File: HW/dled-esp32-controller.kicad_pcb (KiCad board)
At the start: 2 copper layers, 53 x 43 mm, 35 parts, among them J1 PinsI2C, J2 PinsDbg, J3 DLED, J4 swRes, J5 PinsExp, J9 Power5V, Q1 STD46P4LLF6, Q2 IRLML2502, SW1 BootBtn, U1 ESP-WROOM-32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

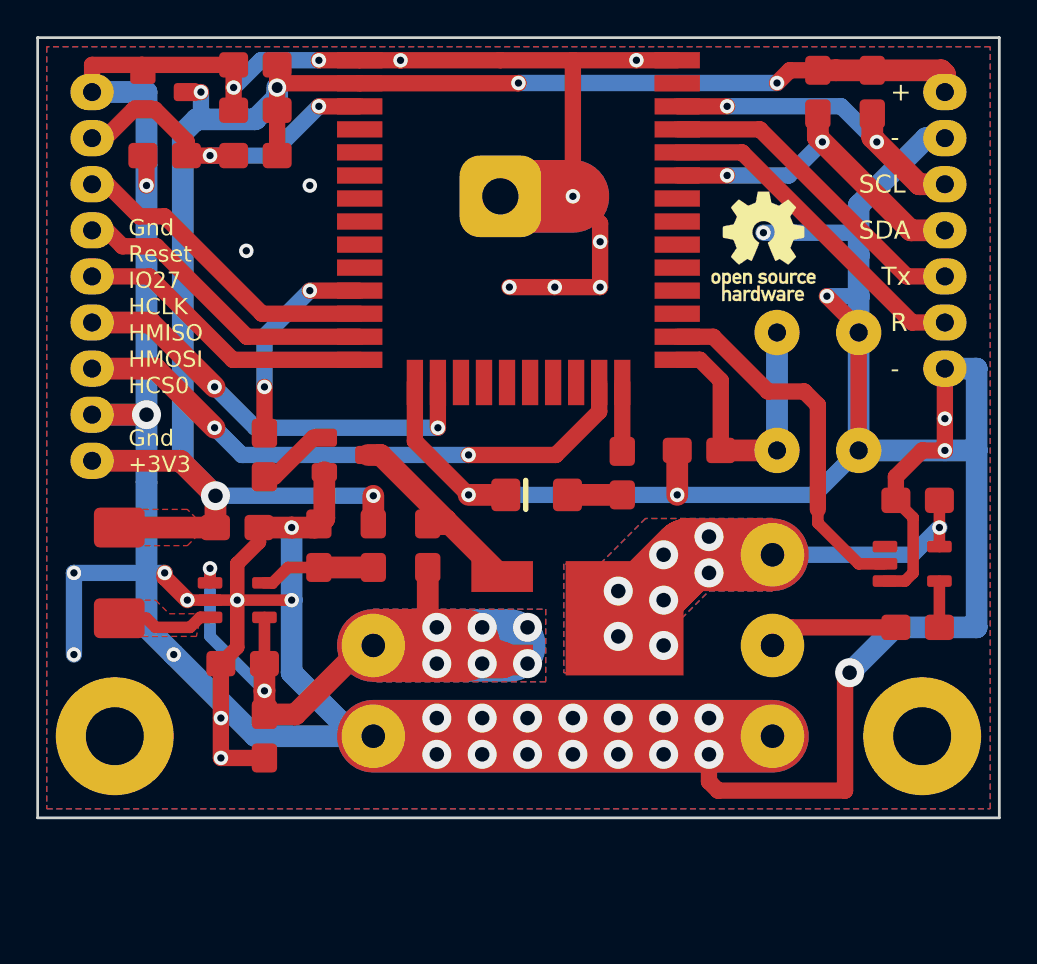
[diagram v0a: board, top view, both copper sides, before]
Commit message: Modifies the design for two outputs
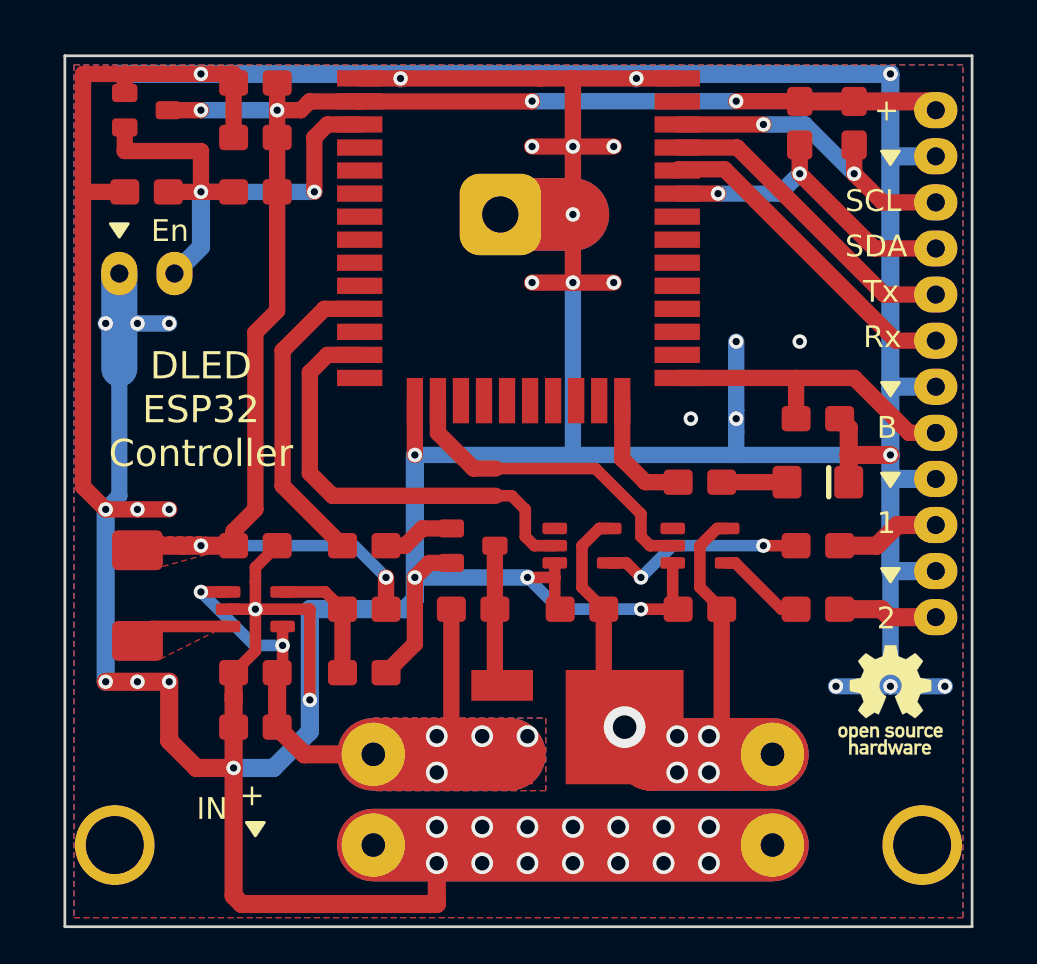
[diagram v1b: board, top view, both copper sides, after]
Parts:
- removed SW1: BootBtn, CalinGeneric:SW-Push-4
- added C9: 100nF, CalinGeneric:C0805HS, F.Cu at (60.0, 82.5)
- added J8: LEDpwr, CalinConnectors:DG301-5-2, F.Cu at (64.0, 93.0)
- added R10: 330, CalinGeneric:R0805HS, F.Cu at (66.5, 82.5)
- added U5: SN74LV1T34, CalinGeneric:SOT-23-5-HS, F.Cu at (60.0, 79.0)
- J3: value DLED -> BootBtn; footprint CalinConnectors:DG301-5-3 -> CalinConnectors:Pin_Header_Straight_1x02
- J5: value PinsExp -> LEDcmd; footprint CalinConnectors:Pin_Header_Straight_1x07 -> CalinConnectors:Pin_Header_Straight_1x03
- U2: value SN74LV1T34 -> BD48K28...30; footprint CalinGeneric:SOT-23-5-HS -> CalinGeneric:SOT-23-HS
- U4: value BD48K28...30 -> SN74LV1T34; footprint CalinGeneric:SOT-23-HS -> CalinGeneric:SOT-23-5-HS
- moved J5 50.1 mm to (73.0, 77.9)
- moved U2 49.0 mm to (29.5, 55.0)
- moved U4 34.0 mm to (53.5, 79.0)
- moved SYM1 26.0 mm to (70.5, 87.5)
- moved C5 19.4 mm to (53.5, 82.5)
- moved D1 15.5 mm to (66.5, 75.5), turned to 180 degrees
- moved J3 14.8 mm to (73.0, 72.8), turned to 0 degrees
- moved J4 8.73 mm to (31.0, 64.0), turned to 270 degrees
- moved Q2 8.60 mm to (47.5, 79.0)
- moved R7 7.43 mm to (41.5, 86.0), turned to 180 degrees
- moved R9 7.43 mm to (41.5, 79.0), turned to 180 degrees
- moved R5 7.11 mm to (66.5, 79.0), turned to 180 degrees
- moved C4 6.78 mm to (66.5, 72.0), turned to 0 degrees
- moved H1 6.00 mm to (27.8, 95.5)
- moved H2 6.00 mm to (72.2, 95.5)
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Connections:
- J3 pad 1: GND -> /Boot
- J3 pad 2: Net-(J3-Pad2) -> GND
- J5 pad 1: /IO27 -> /LEDo1
- J5 pad 2: /HSPICLK -> GND
- J5 pad 3: /HSPIQ -> /LEDo2
- R5 pad 1: Net-(J3-Pad2) -> /LEDo1
- U1 pad 12: /IO27 -> (no net)
- U1 pad 13: /HSPICLK -> /LEDc1
- U1 pad 14: /HSPIQ -> (no net)
- U1 pad 16: /HSPID -> /LEDc2
- U1 pad 23: /HSPICS0 -> (no net)
- U1 pad 26: /LEDcmd -> (no net)
- U2 pad 1: (no net) -> GND
- U2 pad 2: /LEDcmd -> /Reset
- U2 pad 3: GND -> +3V3
- U4 pad 1: GND -> (no net)
- U4 pad 2: /Reset -> /LEDc1
- U4 pad 3: +3V3 -> GND
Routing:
- net GND: track 348.4 -> 413.4 mm, vias 44 -> 49
- net /HSPICS0: track 32.5 -> 0.00 mm, vias 2 -> 0
- net /LEDc1: track 0.00 -> 24.7 mm
- net /HSPID: track 24.0 -> 0.00 mm, vias 2 -> 0
- net /LEDcmd: track 20.4 -> 0.00 mm
- net /LEDc2: track 0.00 -> 18.0 mm
- net /IO27: track 17.7 -> 0.00 mm
- net /HSPICLK: track 17.2 -> 0.00 mm
- net /HSPIQ: track 16.7 -> 0.00 mm
- net +5VL: track 36.4 -> 52.1 mm, vias 8 -> 5
- net +3V3: track 97.9 -> 87.3 mm
- net /Reset: track 19.6 -> 28.5 mm
- net Net-(R5-Pad2): track 2.55 -> 11.4 mm, vias 0 -> 2
- net Net-(J3-Pad2): track 7.21 -> 0.00 mm
- net /LEDo1: track 0.00 -> 5.77 mm
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- removed copper zone on B.Cu, net +5VL
- removed copper zone on F.Cu, net +5VL
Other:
- board size 53 x 43 mm -> 50 x 48 mm
- board text added: "1"
- board text added: "2"
- board text added: "B"
- board text added: "DLED ESP32 Controller"
- board text added: "En"
- board text added: "IN"
- board text added: "Rx"
- board text added: "github.com CalinRadoni dled-esp32-controller"
- board text removed: "-"
- board text removed: "DLED-ESP32-Controller"
- board text removed: "Gnd Reset IO27 HCLK HMISO HMOSI HCS0 Gnd +3V3"
- board text removed: "R"

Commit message: Adds an extension header and improves many PCB traces.
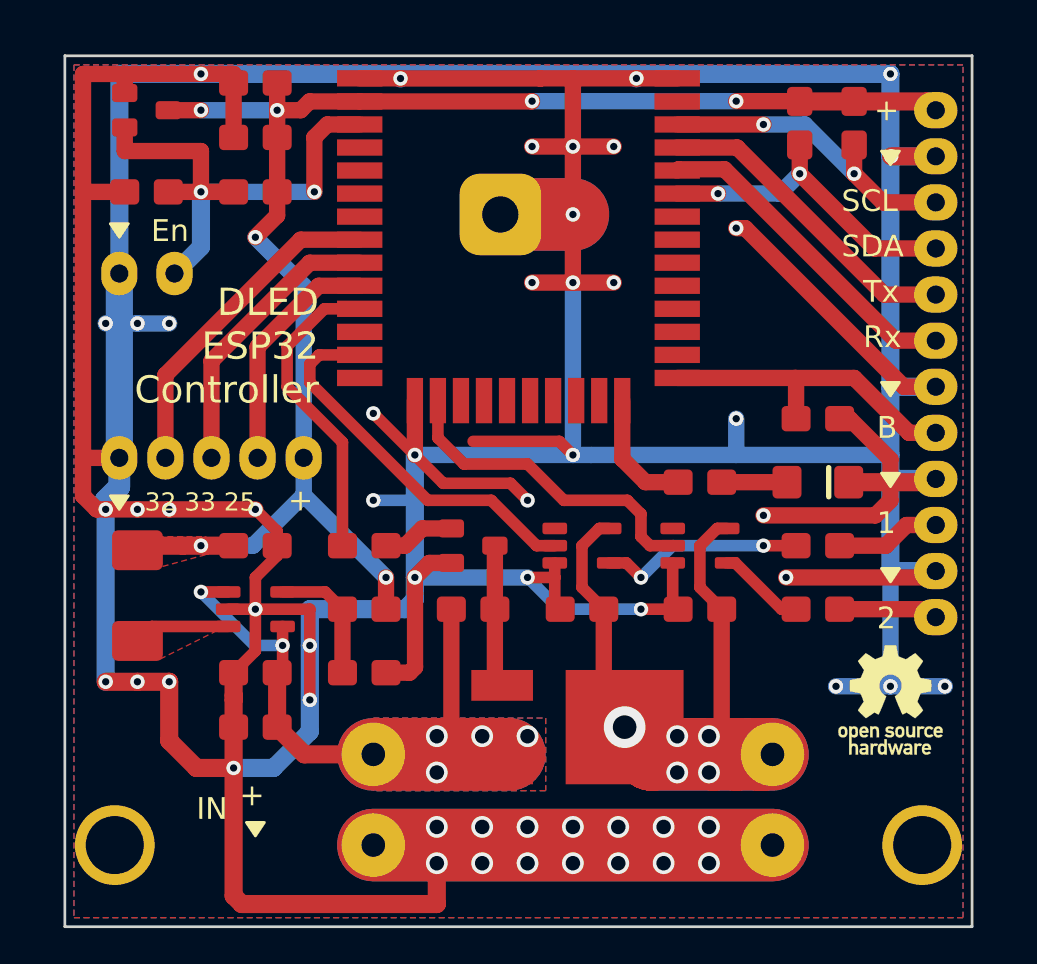
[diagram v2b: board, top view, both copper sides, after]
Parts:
- added J6: PinsExt, CalinConnectors:Pin_Header_Straight_1x05, F.Cu at (28.0, 74.2)
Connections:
- U1 pad 10: (no net) -> /25
- U1 pad 8: (no net) -> /32
- U1 pad 9: (no net) -> /33
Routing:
- net GND: track 413.4 -> 486.7 mm, vias 49 -> 55
- net /32: track 0.00 -> 18.4 mm
- net /33: track 0.00 -> 15.8 mm
- net /25: track 0.00 -> 13.1 mm
- net /LEDc1: track 24.7 -> 21.2 mm
- net +3V3: track 87.3 -> 87.4 mm, vias 6 -> 7
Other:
- board text added: "32 33 25"

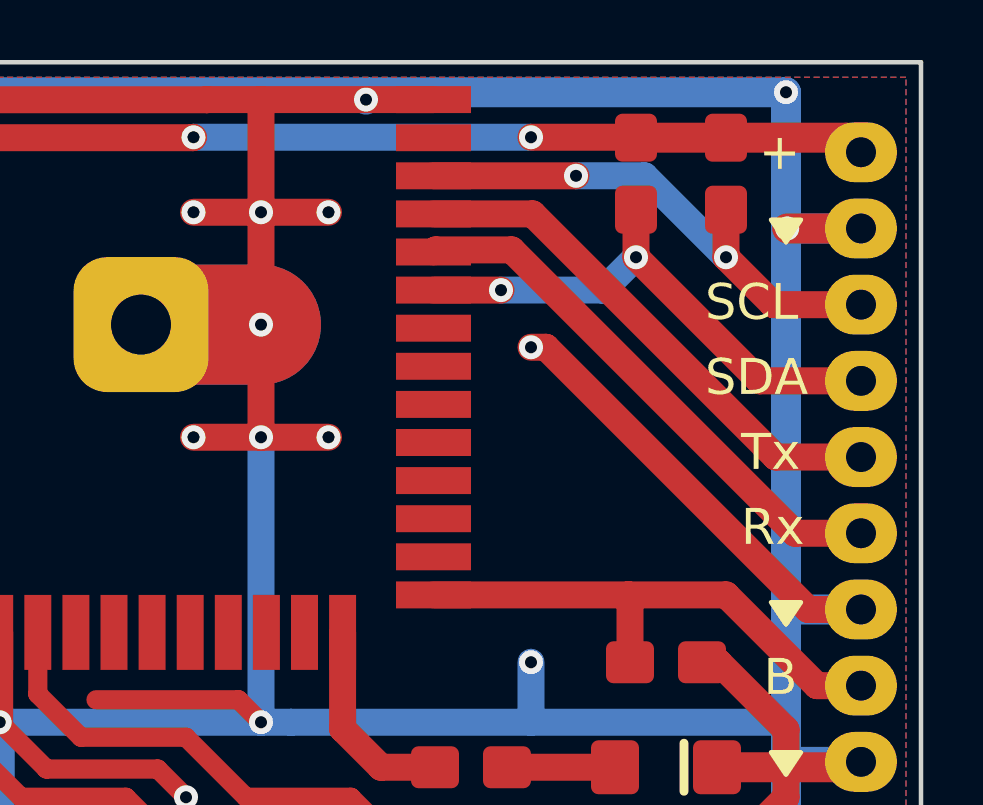
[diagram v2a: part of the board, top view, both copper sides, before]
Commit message: Rebuilds the PCB for the second extension connector
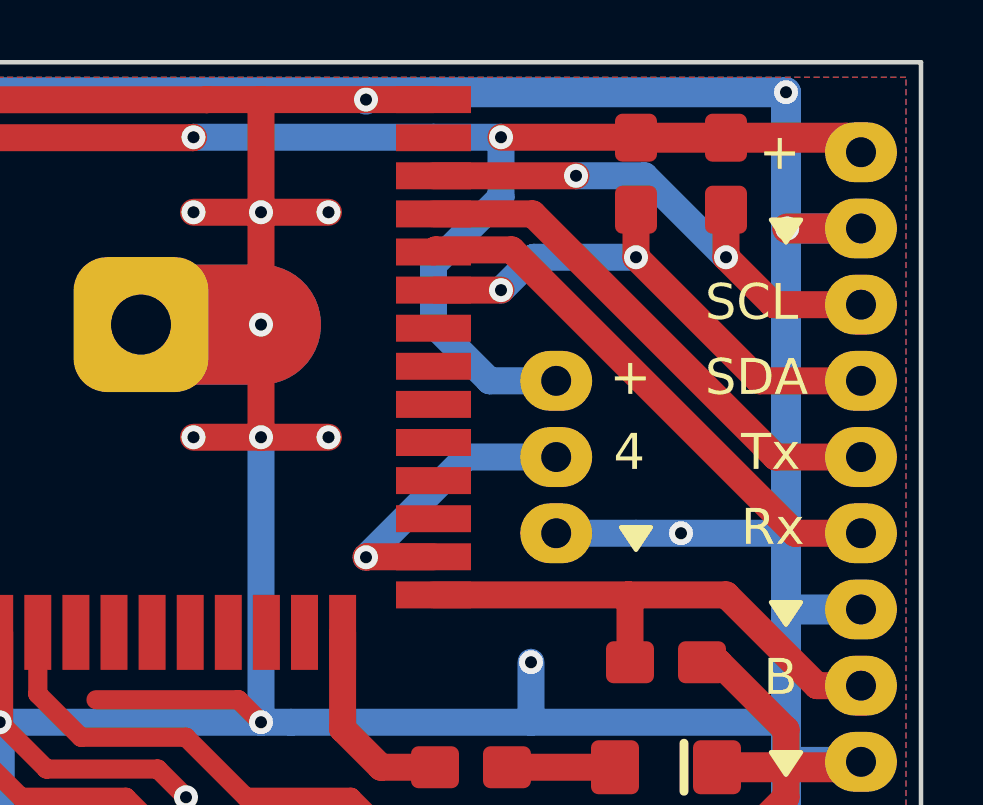
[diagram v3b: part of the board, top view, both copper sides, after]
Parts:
- added J7: PinsExt2, CalinConnectors:Pin_Header_Straight_1x03, F.Cu at (62.8, 62.6)
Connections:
- U1 pad 26: (no net) -> /IO4
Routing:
- net +3V3: track 87.4 -> 99.5 mm
- net /IO4: track 0.00 -> 9.98 mm, vias 0 -> 1
- net GND: track 486.7 -> 479.8 mm
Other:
- board text added: "4"

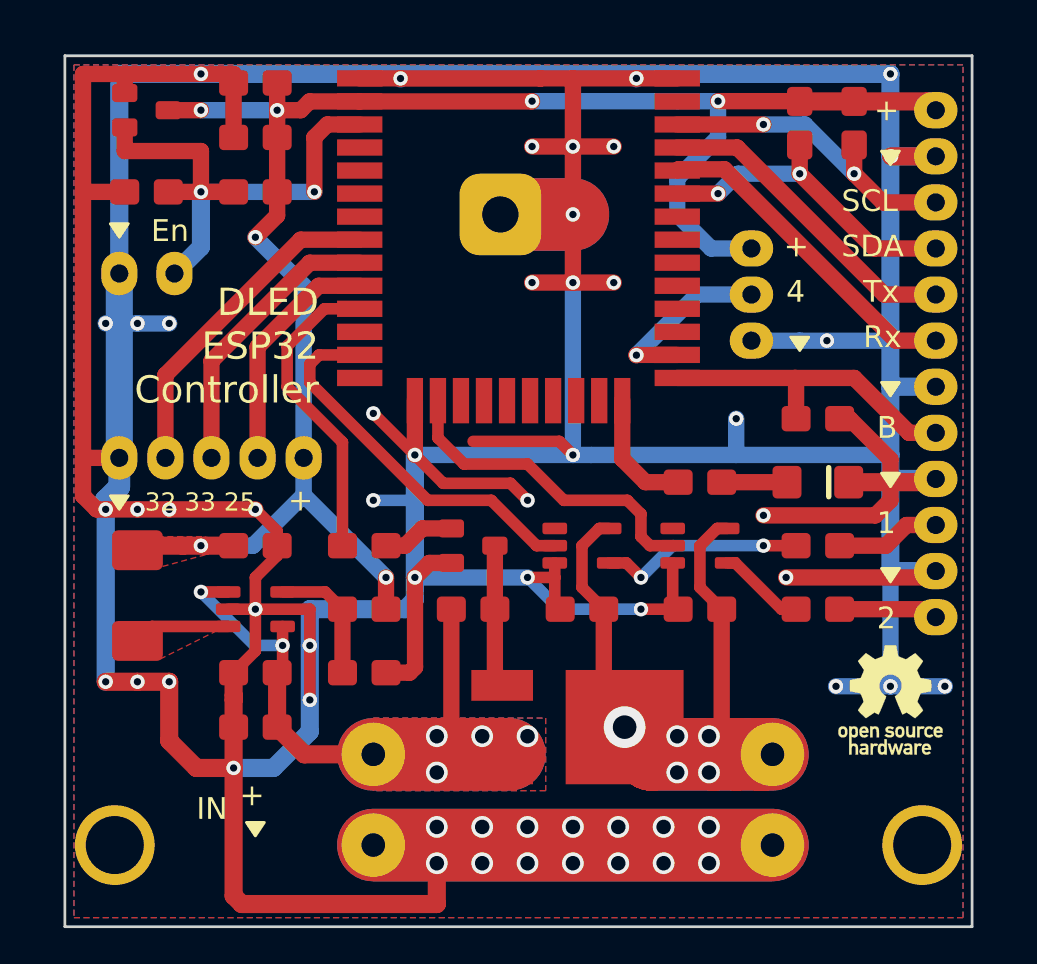
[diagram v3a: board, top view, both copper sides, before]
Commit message: Adjusts the labels for extension connectors
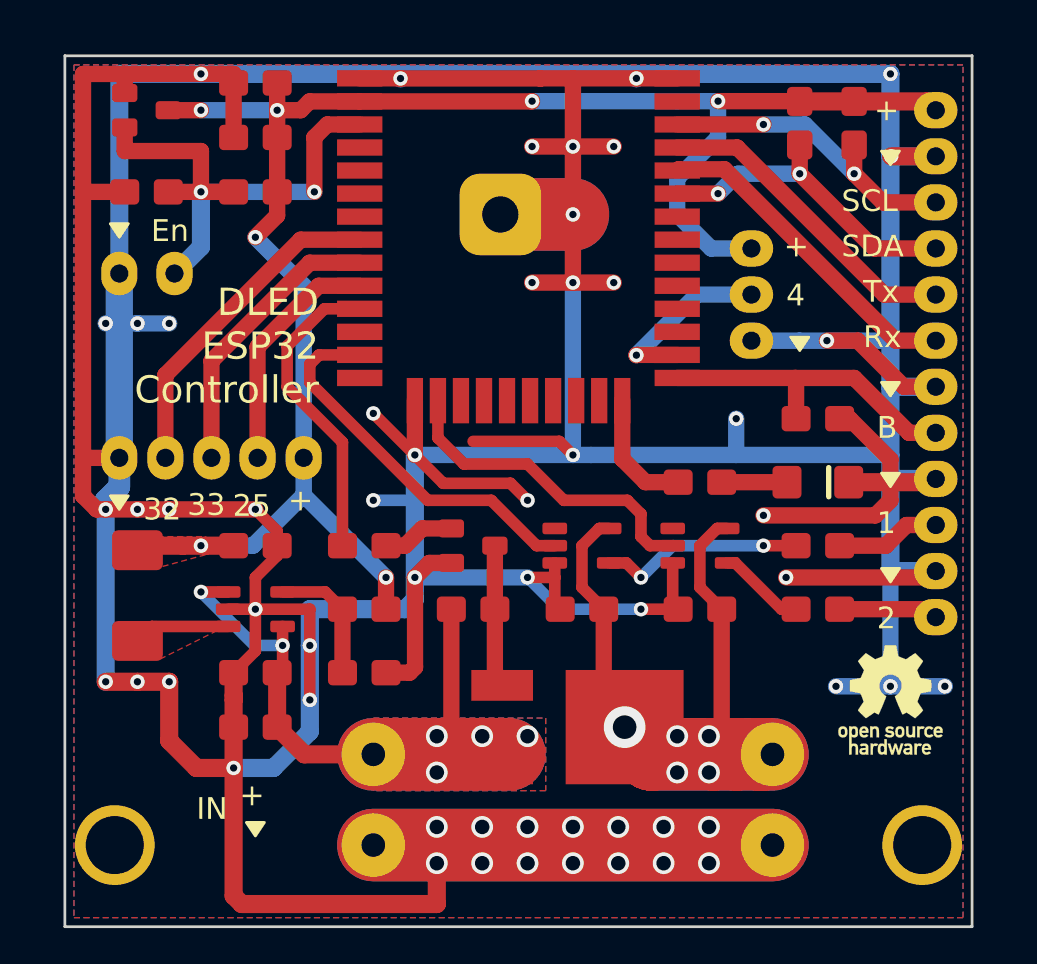
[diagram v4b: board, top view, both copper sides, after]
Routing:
- net GND: track 479.8 -> 486.9 mm
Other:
- board text added: "25"
- board text added: "32"
- board text added: "33"
- board text removed: "32 33 25"
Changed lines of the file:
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@@
   (general
     (thickness 1.6)
-    (drawings 30)
-    (tracks 394)
+    (drawings 32)
+    (tracks 397)
     (zones 0)
     (modules 40)
@@
     )
   )
-  (gr_text 4 (at 64.75 65) (layer F.SilkS)
+  (gr_text 25 (at 34.25 76.8) (layer F.SilkS)
+    (effects (font (size 1.2 1.2) (thickness 0.25)) (justify left))
+  )
+  (gr_text 33 (at 31.75 76.75) (layer F.SilkS)
+    (effects (font (size 1.2 1.2) (thickness 0.25)) (justify left))
+  )
+  (gr_text 4 (at 64.75 65.2) (layer F.SilkS)
     (effects (font (size 1.2 1.2) (thickness 0.25)) (justify left))
   )
@@
   )
   (gr_poly (pts (xy 27.5 76.25) (xy 28.5 76.25) (xy 28 77)) (layer F.SilkS) (width 0.15))
-  (gr_text "32 33 25" (at 29.4 76.6) (layer F.SilkS)
-    (effects (font (size 1 1) (thickness 0.25)) (justify left))
+  (gr_text 32 (at 29.32 77) (layer F.SilkS)
+    (effects (font (size 1.2 1.2) (thickness 0.25)) (justify left))
   )
   (gr_text IN (at 32.25 93.5) (layer F.SilkS)
@@
   (segment (start 65.5 67.7) (end 70.45 67.7) (width 0.9) (layer B.Cu) (net 1))
   (via (at 67 67.7) (size 0.8) (drill 0.4) (layers F.Cu B.Cu) (net 1))
+  (segment (start 67 67.7) (end 68.7 67.7) (width 0.9) (layer F.Cu) (net 1))
+  (segment (start 71.24 70.24) (end 73 70.24) (width 0.9) (layer F.Cu) (net 1))
+  (segment (start 68.7 67.7) (end 71.24 70.24) (width 0.9) (layer F.Cu) (net 1))
   (via (at 32.5 59.5) (size 0.8) (drill 0.4) (layers F.Cu B.Cu) (net 2))
   (via (at 38.75 59.5) (size 0.8) (drill 0.4) (layers F.Cu B.Cu) (net 2))

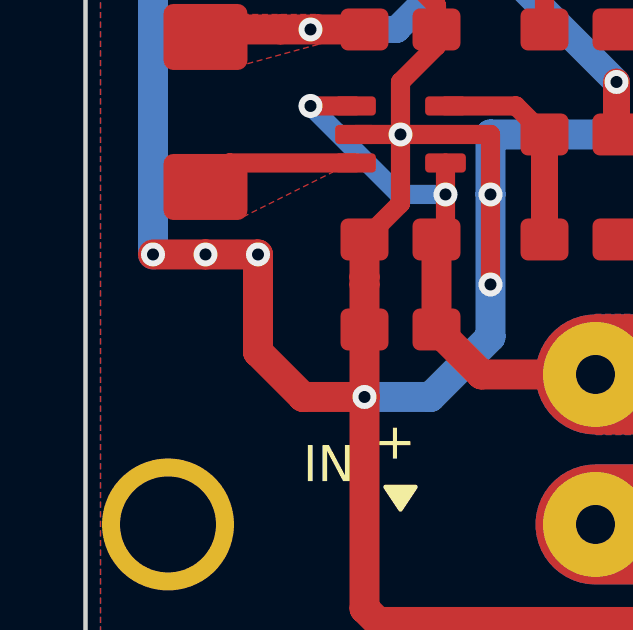
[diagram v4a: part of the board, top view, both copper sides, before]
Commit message: Adds revision info for PCB and updates README.md for version 0.9
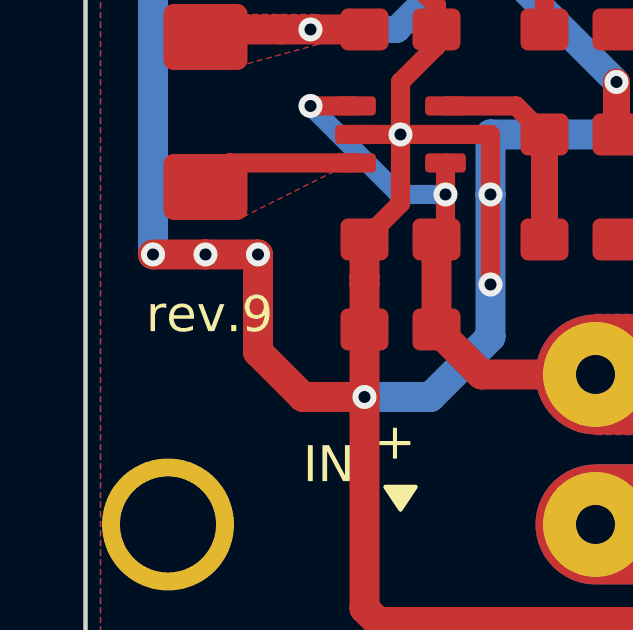
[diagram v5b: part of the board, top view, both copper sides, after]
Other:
- board text added: "rev.9"
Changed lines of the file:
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@@
   (general
     (thickness 1.6)
-    (drawings 32)
+    (drawings 33)
     (tracks 397)
     (zones 0)
@@
   )
   (setup
-    (last_trace_width 0.9)
+    (last_trace_width 0.35)
     (user_trace_width 0.35)
     (user_trace_width 0.6)
@@
     )
   )
+  (gr_text rev.9 (at 31.25 88.5) (layer F.SilkS)
+    (effects (font (size 1.2 1.2) (thickness 0.25)) (justify right))
+  )
   (gr_text 25 (at 34.25 76.8) (layer F.SilkS)
